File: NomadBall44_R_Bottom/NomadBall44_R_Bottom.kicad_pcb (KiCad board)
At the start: 2 copper layers, 527.6 x 105.9 mm, 11 parts

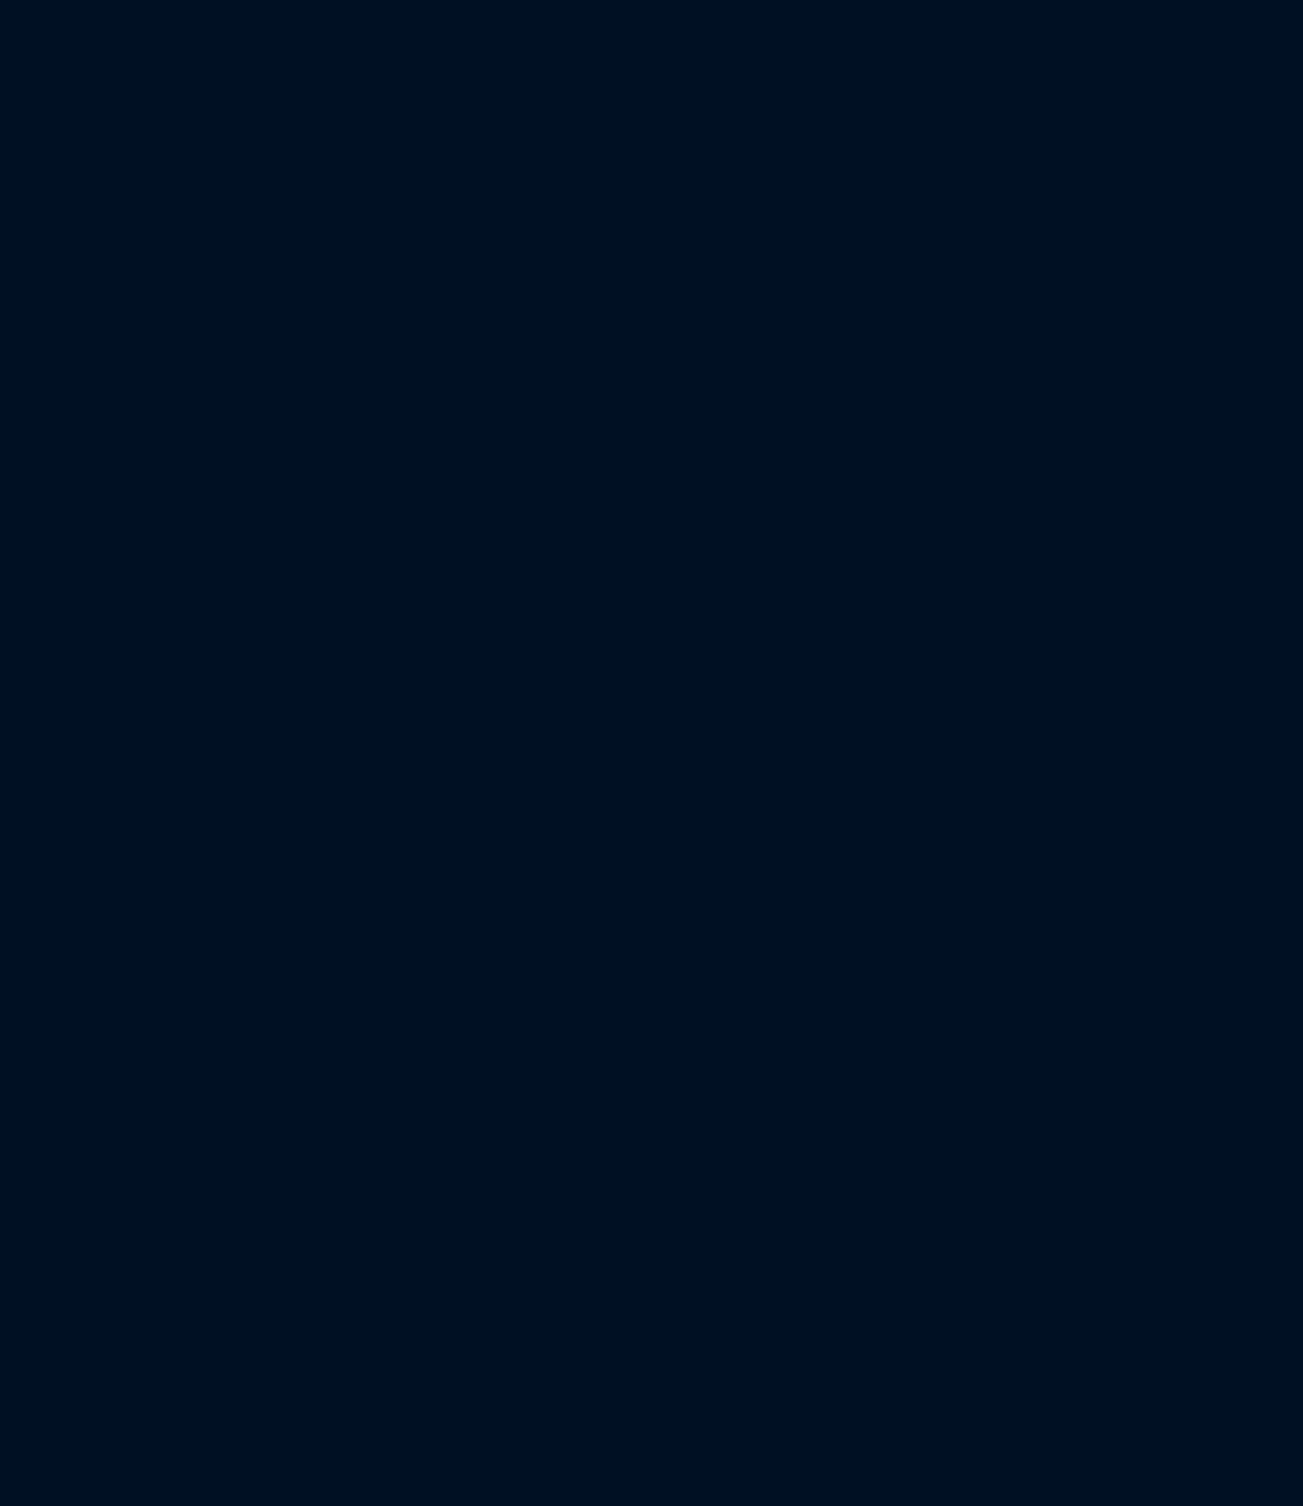
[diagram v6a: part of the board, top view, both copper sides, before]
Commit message: keyballのボトムケースデータを読み込み
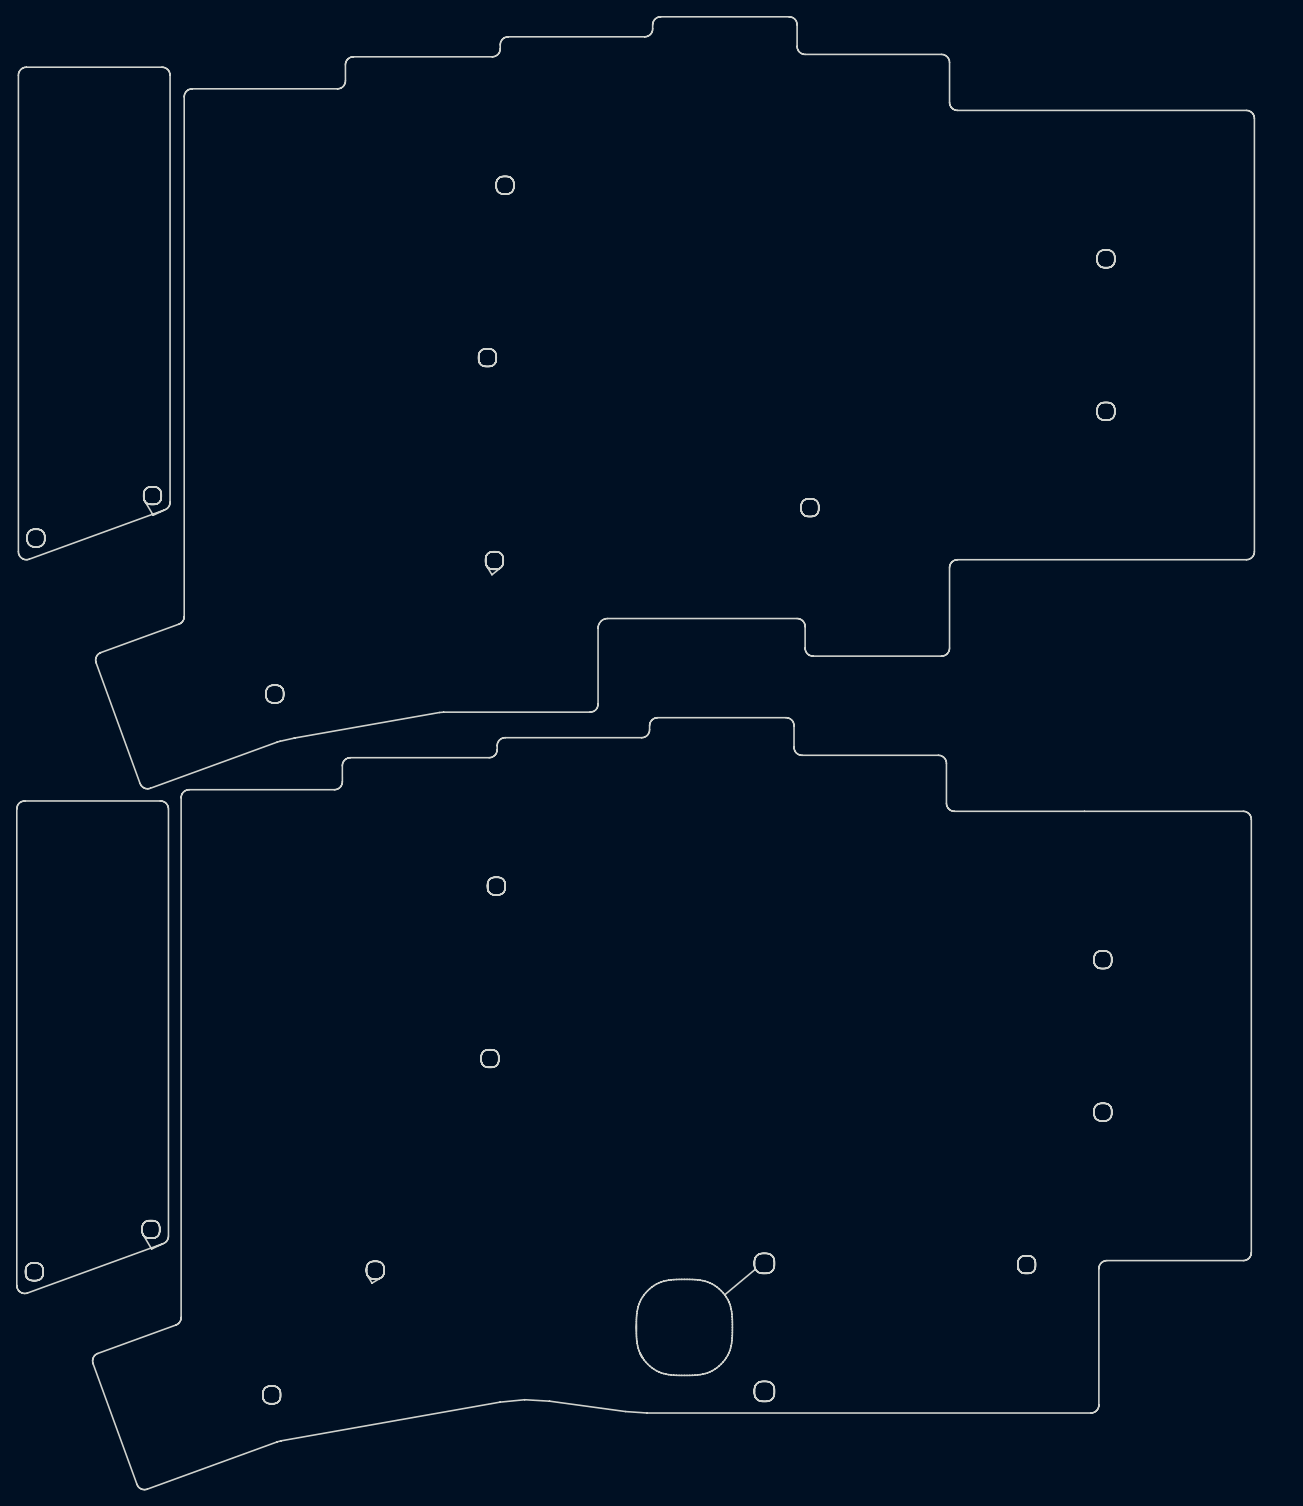
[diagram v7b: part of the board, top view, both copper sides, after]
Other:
- board size 527.6 x 105.9 mm -> 764.7 x 184.1 mm

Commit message: m1.9用のネジ穴を追加 & PHコネクタ用のエリアを修正
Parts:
- added REF**: Val**, NomadBall44:m1.9_Screw_Hole_EdgeCuts, F.Cu at (159.7, 124.9)
- added REF**: Val**, NomadBall44:m1.9_Screw_Hole_EdgeCuts, F.Cu at (159.7, 108.9)
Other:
- board size 764.7 x 184.1 mm -> 147.4 x 87.5 mm
